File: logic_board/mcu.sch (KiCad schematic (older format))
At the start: 15 parts, among them J1 SWD, J6 Serial, SW1 TL3315NF160Q, SW2 TL3315NF160Q, SW3 TL3315NF160Q, SW4 TL3315NF160Q, U1 STM32G474CET6, Y1 8 MHz

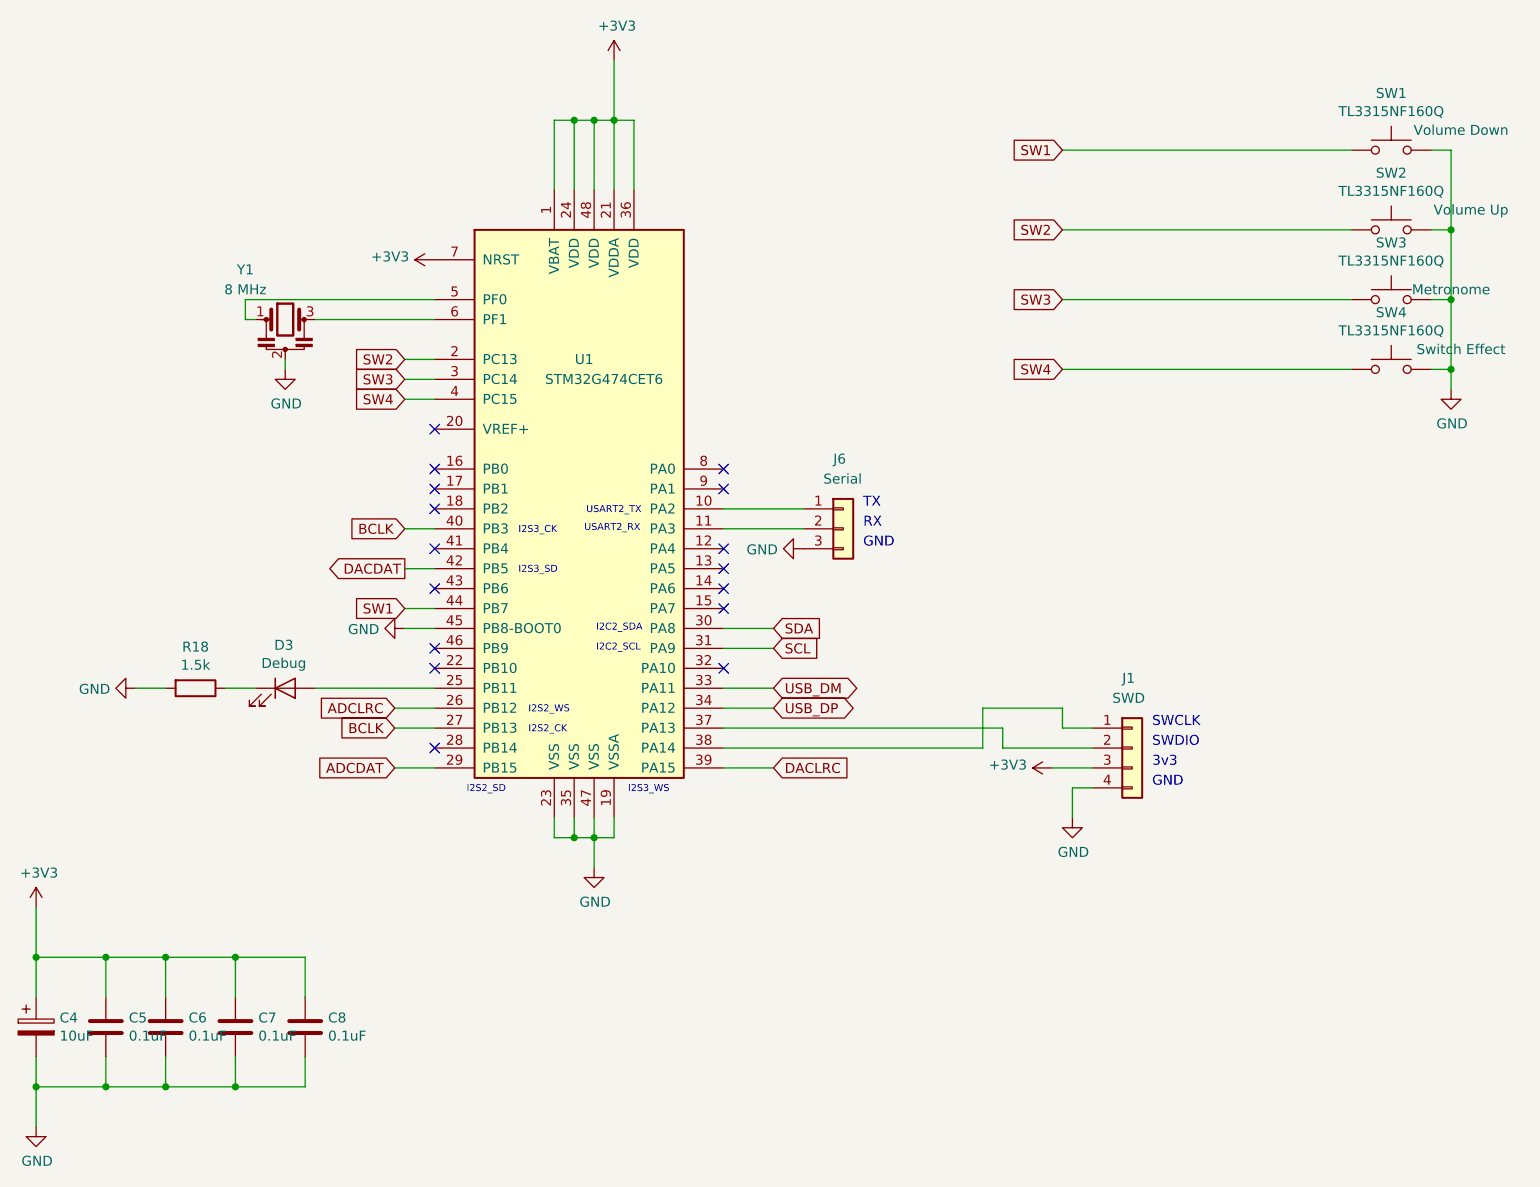
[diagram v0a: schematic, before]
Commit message: Swap MCU resonator so the input/outputs are connected correctly.
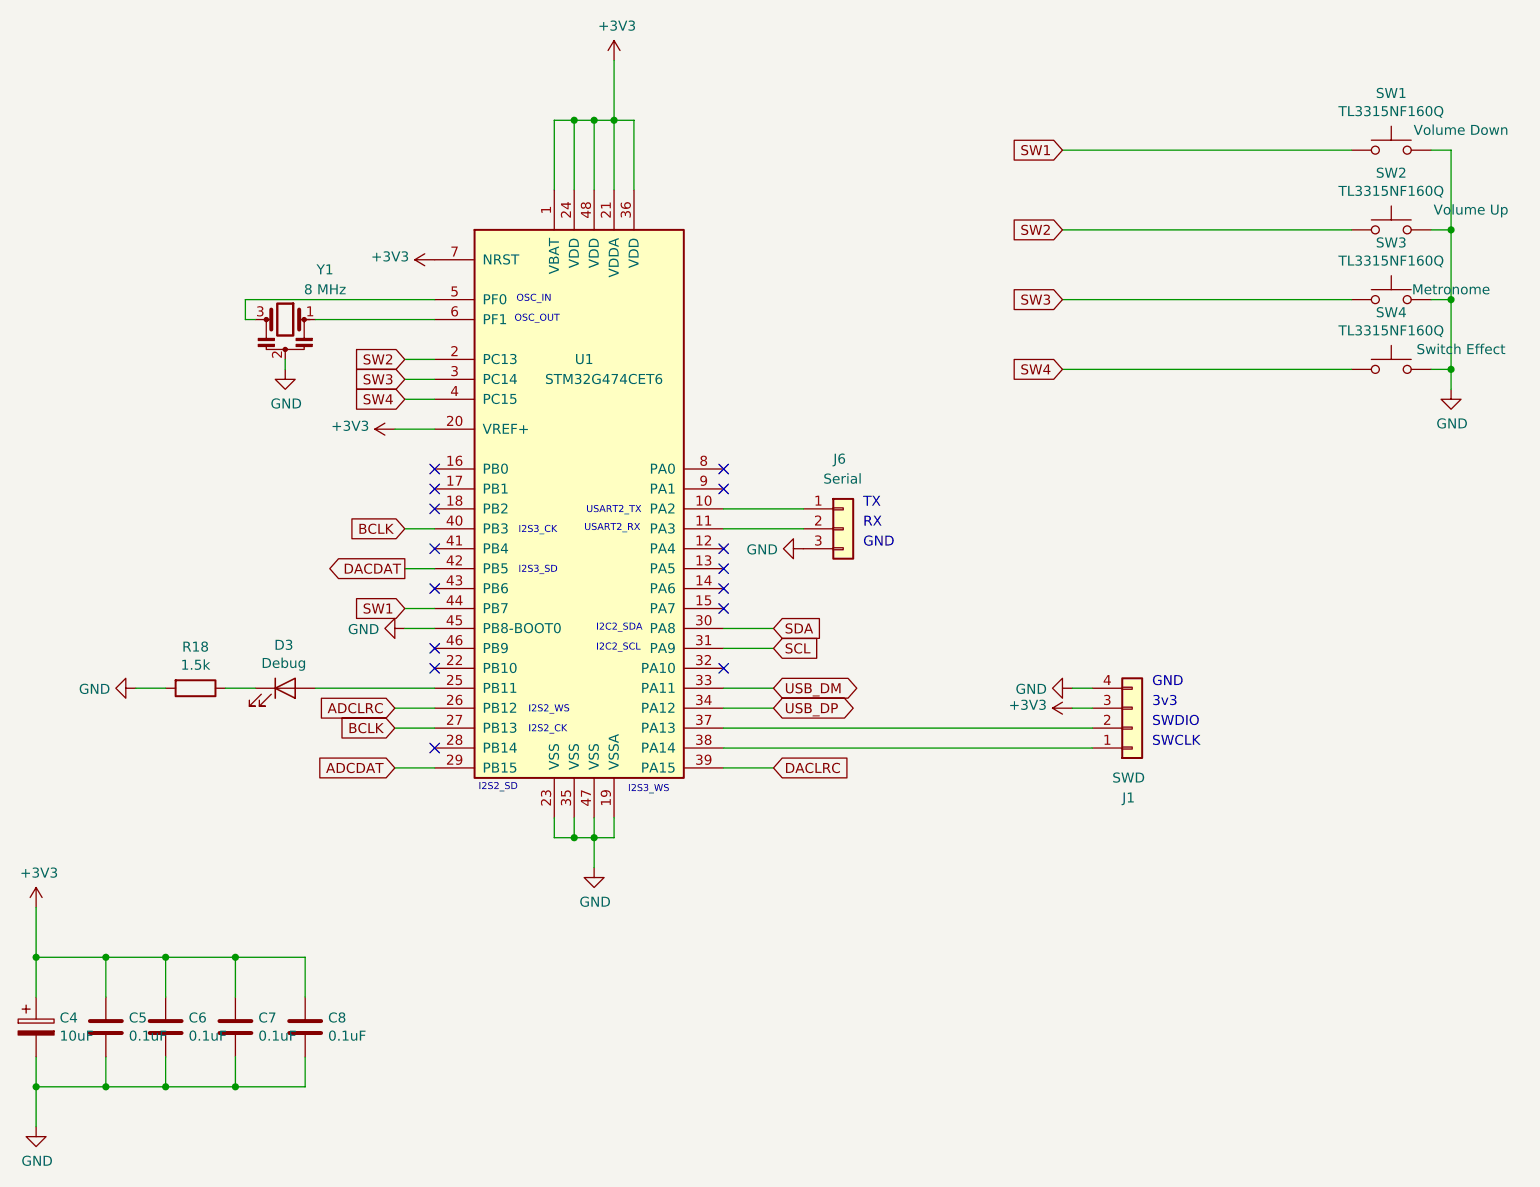
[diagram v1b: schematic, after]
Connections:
- net +3V3: now also U1.20 (VREF+)
- net at Y1.1: now also U1.6 (PF1); no longer U1.5 (PF0)
- net at Y1.3: now also U1.5 (PF0); no longer U1.6 (PF1)
- no-connect marks 16 -> 15
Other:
- note added: "OSC_IN"
- note added: "OSC_OUT"
- moved on the sheet: J1
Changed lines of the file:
@@
 	2700 6900 2700 6700
-$Comp
-L power:GND #PWR011
-U 1 1 5E3784CF
-P 7900 5350
-F 0 "#PWR011" H 7900 5100 50  0001 C CNN
-F 1 "GND" H 7905 5177 50  0000 C CNN
-F 2 "" H 7900 5350 50  0001 C CNN
-F 3 "" H 7900 5350 50  0001 C CNN
-	1    7900 5350
-	1    0    0    -1
-$EndComp
-Wire Wire Line
-	7900 5350 7900 5200
-Wire Wire Line
-	7900 5200 8000 5200
 $Comp
 L power:+3V3 #PWR010
 U 1 1 5E40AE38
-P 7800 5100
-F 0 "#PWR010" H 7800 4950 50  0001 C CNN
-F 1 "+3V3" V 7815 5228 50  0000 L CNN
-F 2 "" H 7800 5100 50  0001 C CNN
-F 3 "" H 7800 5100 50  0001 C CNN
-	1    7800 5100
+P 7900 4800
+F 0 "#PWR010" H 7900 4650 50  0001 C CNN
+F 1 "+3V3" V 7915 4928 50  0000 L CNN
+F 2 "" H 7900 4800 50  0001 C CNN
+F 3 "" H 7900 4800 50  0001 C CNN
+	1    7900 4800
 	0    -1   -1   0
 $EndComp
-Wire Wire Line
-	7800 5100 8000 5100
 Wire Wire Line
 	9700 2000 9800 2000
@@
 F 3 "~" H 3925 2850 50  0001 C CNN
 	1    3950 2850
-	1    0    0    -1
+	-1   0    0    -1
 $EndComp
 $Comp
@@
 L Connector_Generic:Conn_01x04 J1
 U 1 1 5E4DEDD9
-P 8200 5000
-F 0 "J1" H 8150 5350 50  0000 L CNN
-F 1 "SWD" H 8100 5250 50  0000 L CNN
-F 2 "Pin_Headers:Pin_Header_Straight_1x04_Pitch2.54mm" H 8200 5000 50  0001 C CNN
-F 3 "~" H 8200 5000 50  0001 C CNN
-	1    8200 5000
-	1    0    0    -1
-$EndComp
-Text Notes 8300 5000 0    50   ~ 0
+P 8200 4900
+F 0 "J1" H 8150 5250 50  0000 L CNN
+F 1 "SWD" H 8100 5150 50  0000 L CNN
+F 2 "Pin_Headers:Pin_Header_Straight_1x04_Pitch2.54mm" H 8200 4900 50  0001 C CNN
+F 3 "~" H 8200 4900 50  0001 C CNN
+	1    8200 4900
+	1    0    0    1
+$EndComp
+Text Notes 8300 4900 0    50   ~ 0
 SWDIO
 Wire Wire Line
@@
 Wire Wire Line
 	6150 4500 6400 4500
-Wire Wire Line
-	7550 4900 7550 5000
-Wire Wire Line
-	7550 5000 8000 5000
-Wire Wire Line
-	6150 5000 7450 5000
-Wire Wire Line
-	7450 5000 7450 4800
-Wire Wire Line
-	7450 4800 7850 4800
-Wire Wire Line
-	7850 4800 7850 4900
-Wire Wire Line
-	7850 4900 8000 4900
-NoConn ~ 4700 3400
 NoConn ~ 4700 3600
 NoConn ~ 4700 3700
@@
 	0    1    1    0
 $EndComp
-Text Notes 8300 4900 0    50   ~ 0
+Text Notes 8300 5000 0    50   ~ 0
 SWCLK
-Text Notes 8300 5100 0    50   ~ 0
+Text Notes 8300 4800 0    50   ~ 0
 3v3
-Text Notes 8300 5200 0    50   ~ 0
+Text Notes 8300 4700 0    50   ~ 0
 GND
 Text Notes 6850 3800 0    50   ~ 0
@@
 Wire Wire Line
 	4500 5100 4700 5100
-Text Notes 4860 5230 0    35   ~ 0
+Text Notes 4920 5220 0    35   ~ 0
 I2S2_SD
 Wire Wire Line
@@
 	7850 3100 9300 3100
 Wire Wire Line
-	6150 4900 7550 4900
-Wire Wire Line
 	5400 1850 5300 1850
 Wire Wire Line
 	5300 1850 5300 2200
 Connection ~ 5400 1850
+$Comp
+L power:+3V3 #PWR0108
+U 1 1 5E3FFADC
+P 4500 3400
+F 0 "#PWR0108" H 4500 3250 50  0001 C CNN
+F 1 "+3V3" V 4515 3528 50  0000 L CNN
+F 2 "" H 4500 3400 50  0001 C CNN
+F 3 "" H 4500 3400 50  0001 C CNN
+	1    4500 3400
+	0    -1   -1   0
+$EndComp
+Wire Wire Line
+	4500 3400 4700 3400
+Wire Wire Line
+	6150 5000 8000 5000
+Wire Wire Line
+	6150 4900 8000 4900
+$Comp
+L power:GND #PWR?
+U 1 1 5E423761
+P 7900 4700
+F 0 "#PWR?" H 7900 4450 50  0001 C CNN
+F 1 "GND" V 7905 4572 50  0000 R CNN
+F 2 "" H 7900 4700 50  0001 C CNN
+F 3 "" H 7900 4700 50  0001 C CNN
+	1    7900 4700
+	0    1    1    0
+$EndComp
+Wire Wire Line
+	7900 4800 8000 4800
+Wire Wire Line
+	7900 4700 8000 4700
+Text Notes 5110 2770 0    35   ~ 0
+OSC_IN
+Text Notes 5100 2870 0    35   ~ 0
+OSC_OUT
 $EndSCHEMATC

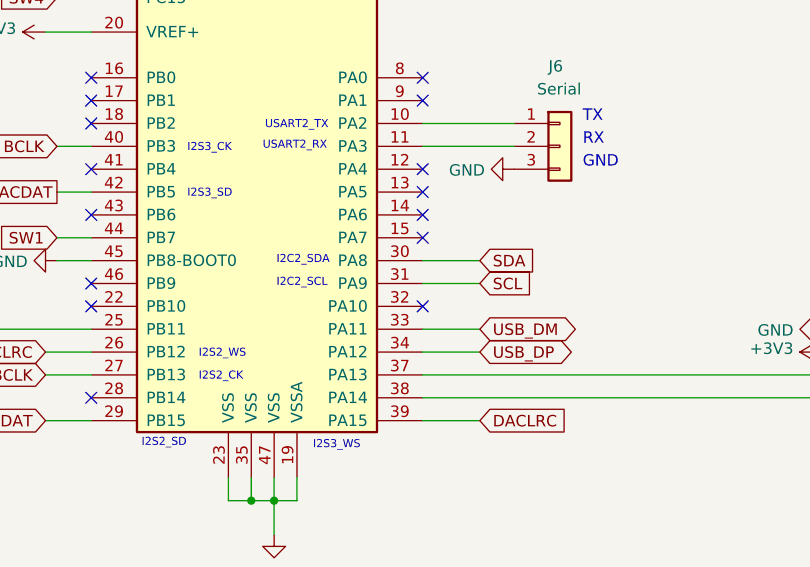
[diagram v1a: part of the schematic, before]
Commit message: Move I2C2_SDA from PA8 to PA10
There is conflicting information in the datahsheet. Table 13 says this
should be PA10, but Table 12 says PA8. I'm using the former, as it
has actual mappings. This would be fairly easy to rework with a blue
wire if I guessed wrong: jumpering the pins together and making PA10
be an input.
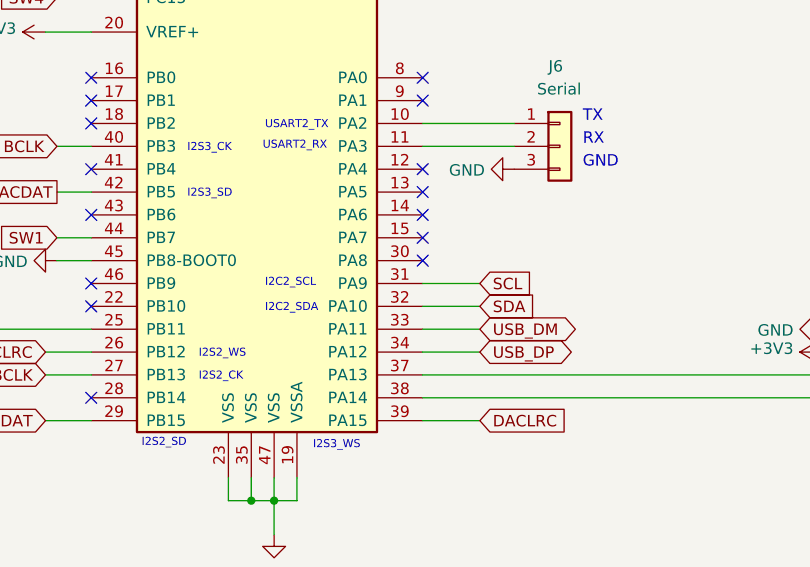
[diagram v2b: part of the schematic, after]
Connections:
- net SDA: now also U1.32 (PA10); no longer U1.30 (PA8)
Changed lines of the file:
@@
 Wire Wire Line
 	4550 4300 4700 4300
-Text GLabel 6400 4400 2    50   Input ~ 0
+Text GLabel 6400 4600 2    50   Input ~ 0
 SDA
 Text GLabel 6400 4500 2    50   Input ~ 0
 SCL
-Wire Wire Line
-	6150 4400 6400 4400
 Wire Wire Line
 	6150 4500 6400 4500
@@
 NoConn ~ 6150 4200
 NoConn ~ 6150 4300
-NoConn ~ 6150 4600
 $Comp
 L power:GND #PWR0105
@@
 Text Notes 5450 3920 0    35   ~ 0
 USART2_RX
-Text Notes 5510 4420 0    35   ~ 0
+Text Notes 5460 4630 0    35   ~ 0
 I2C2_SDA
-Text Notes 5510 4520 0    35   ~ 0
+Text Notes 5460 4520 0    35   ~ 0
 I2C2_SCL
 $Comp
@@
 Text Notes 5100 2870 0    35   ~ 0
 OSC_OUT
+Wire Wire Line
+	6150 4600 6400 4600
+NoConn ~ 6150 4400
 $EndSCHEMATC
